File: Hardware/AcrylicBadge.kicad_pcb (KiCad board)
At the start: 2 copper layers, 68.6 x 28 mm, 55 parts, among them J1 CellP, J2 CellN, J3 Conn_02x03_Odd_Even, J4 USB4125-GF-A, U1 ATmega328PB-AU, U2 PAM2401SCADJ, U3 MCP73833T-AMI/UN, U4 BQ29737, U5 CSD16406Q3, U6 CSD16406Q3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

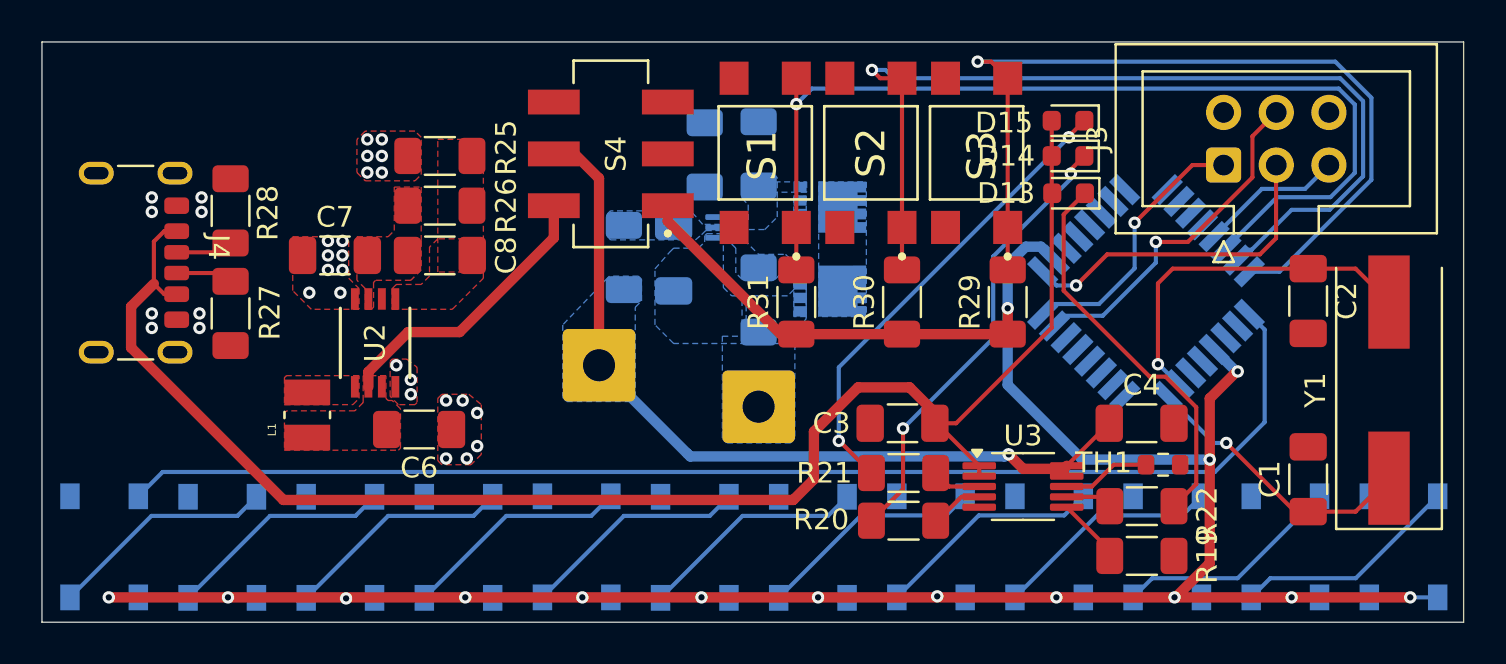
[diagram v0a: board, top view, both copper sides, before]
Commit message: Finished PCB layout
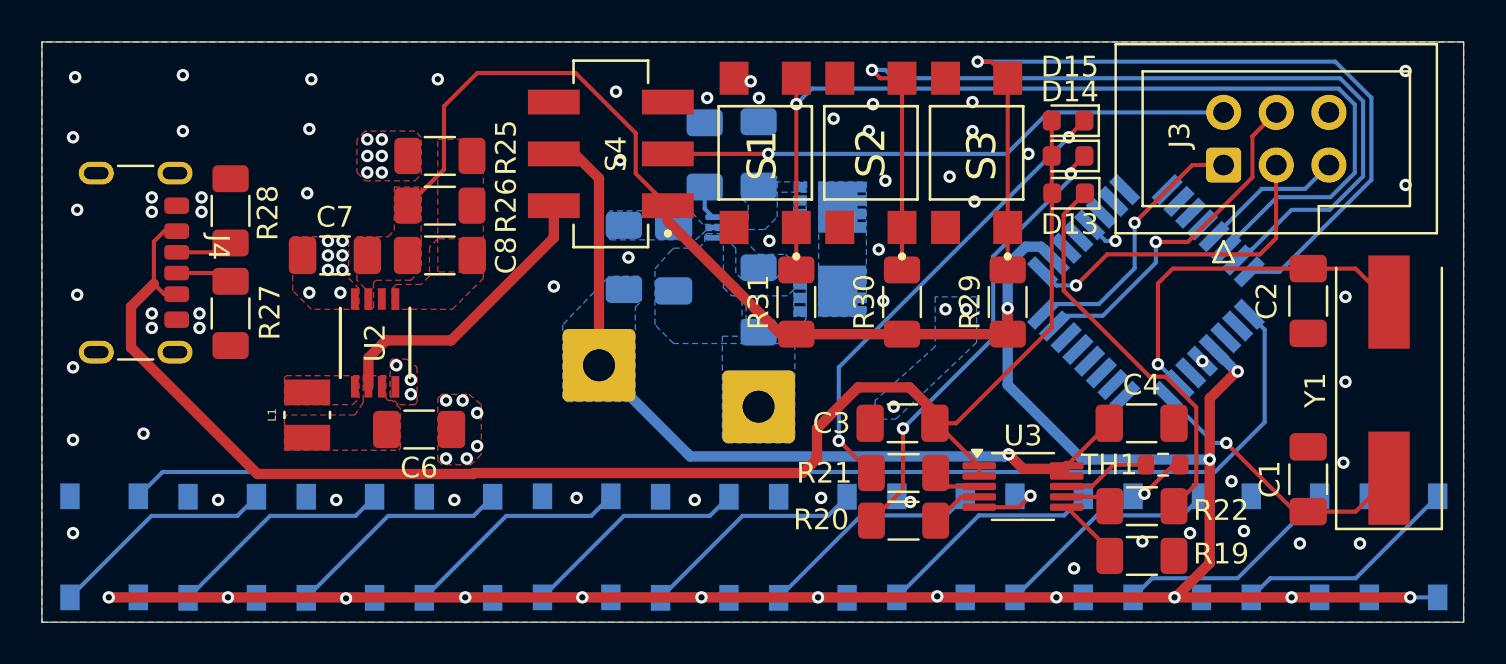
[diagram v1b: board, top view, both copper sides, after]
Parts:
- renumbered J1 to LiPo+, J2 to LiPo-
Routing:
- net programmer_vcc: track 0.00 -> 27.6 mm, vias 0 -> 1
- net avr_vcc: track 133.5 -> 154.3 mm
- net GND: track 0.00 -> 6.58 mm, vias 31 -> 90
- net Net-(U4-V-): track 0.00 -> 1.62 mm
- net Net-(D13-A): track 75.7 -> 74.1 mm
